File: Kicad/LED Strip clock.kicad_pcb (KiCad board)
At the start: 2 copper layers, 142.2 x 116.8 mm, 109 parts, among them J1 Conn_01x09_Male, J2 Conn_01x09_Male, J3 Conn_01x09_Male, J4 Conn_01x09_Male, J5 Conn_01x09_Male, J6 Conn_01x09_Male, J7 Barrel_Jack_Switch, J8 Conn_01x18_Male, U1 TPIC6B595, U10 WeMos_D1_mini, U11 MCP23008-xSO, U12 INA219AxD, U13 DS3231MZ, U2 TPIC6B595, U3 TPIC6B595, U4 TPIC6B595, U5 TPIC6B595, U6 TPIC6B595, U7 MAX809S, U8 74HCT244, U9 L7805

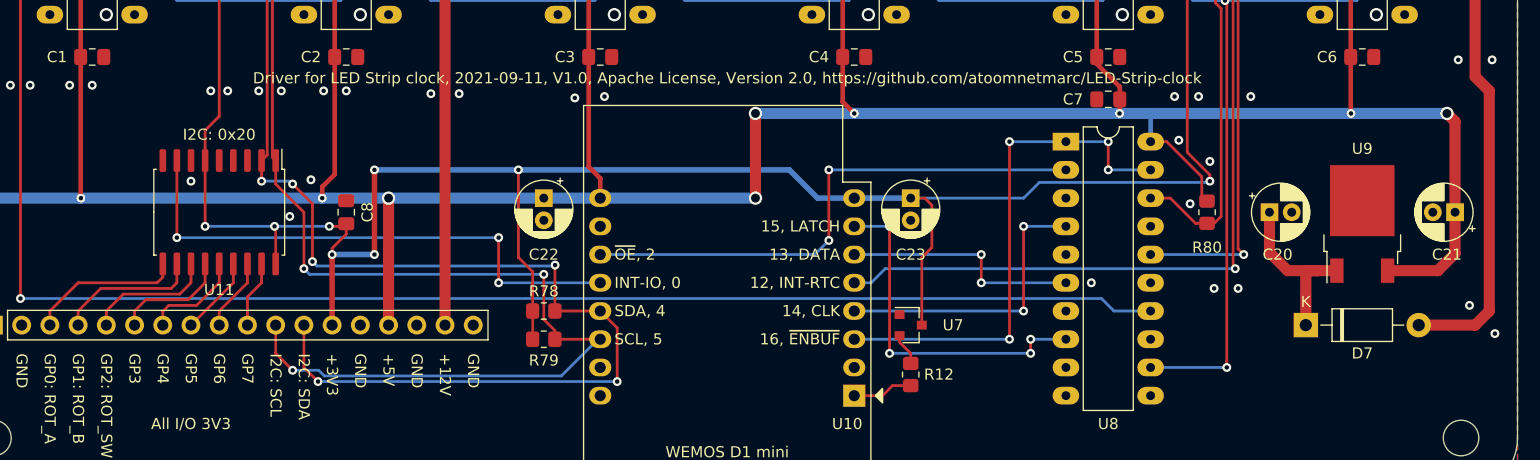
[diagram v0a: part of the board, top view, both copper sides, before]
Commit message: Change footprint of 7805 to D2PAK.
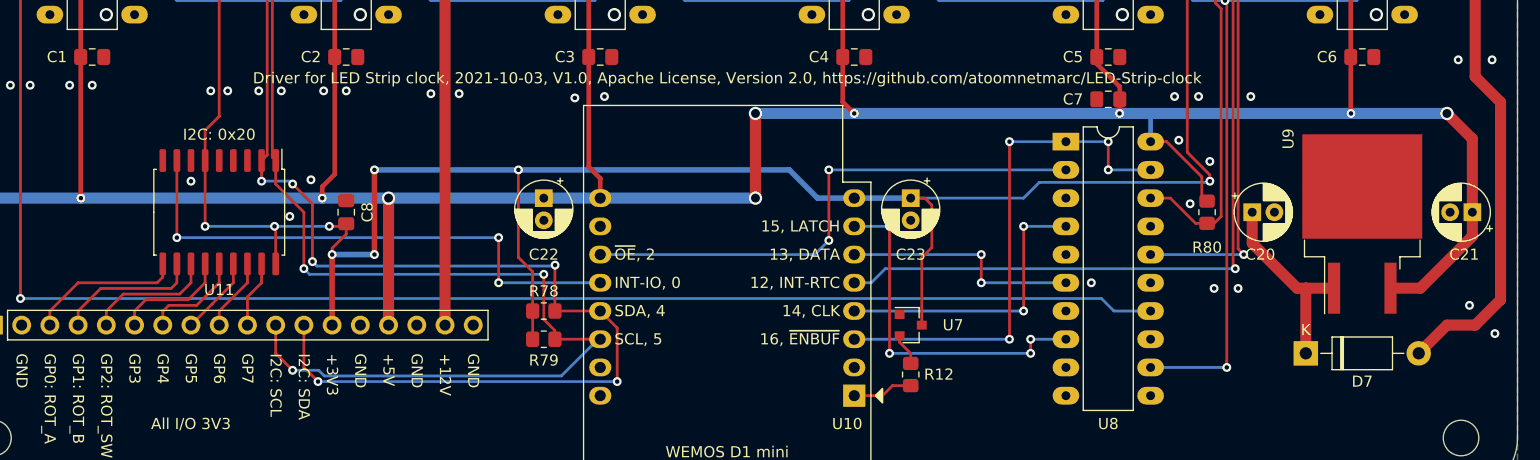
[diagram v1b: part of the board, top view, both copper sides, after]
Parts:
- U9: footprint Package_TO_SOT_SMD:TO-252-2 -> Package_TO_SOT_SMD:TO-263-2
- moved D7 2.54 mm to (204.5, 134.6)
- moved C20 1.56 mm to (199.6, 121.9)
- moved C21 1.56 mm to (219.5, 121.9)
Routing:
- net +12V: track 515.8 -> 517.7 mm
- net +5V: track 423.6 -> 425.3 mm
- net Net-(C20-Pad1): track 16.4 -> 17.7 mm
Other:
- board text added: "Driver for LED Strip clock, 2021-10-03, V1.0, Apache License, Version 2.0, https://github.com/atoomnetmarc/LED-Strip-clock"
- board text removed: "Driver for LED Strip clock, 2021-09-11, V1.0, Apache License, Version 2.0, https://github.com/atoomnetmarc/LED-Strip-clock"
